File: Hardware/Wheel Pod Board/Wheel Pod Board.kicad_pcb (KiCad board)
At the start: 2 copper layers, 63.5 x 25.5 mm, 30 parts, among them J1 Conn_RJ-45, P1 UIM240XX_Stepper_Conn, P2 RS232, P3 ST_SWD_Connector, P4 SyRen, P5 BATT, U1 STM32F401RCT6, U2 SN75176BDR, U3 ZXCT1107, U4 ZXCT1107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

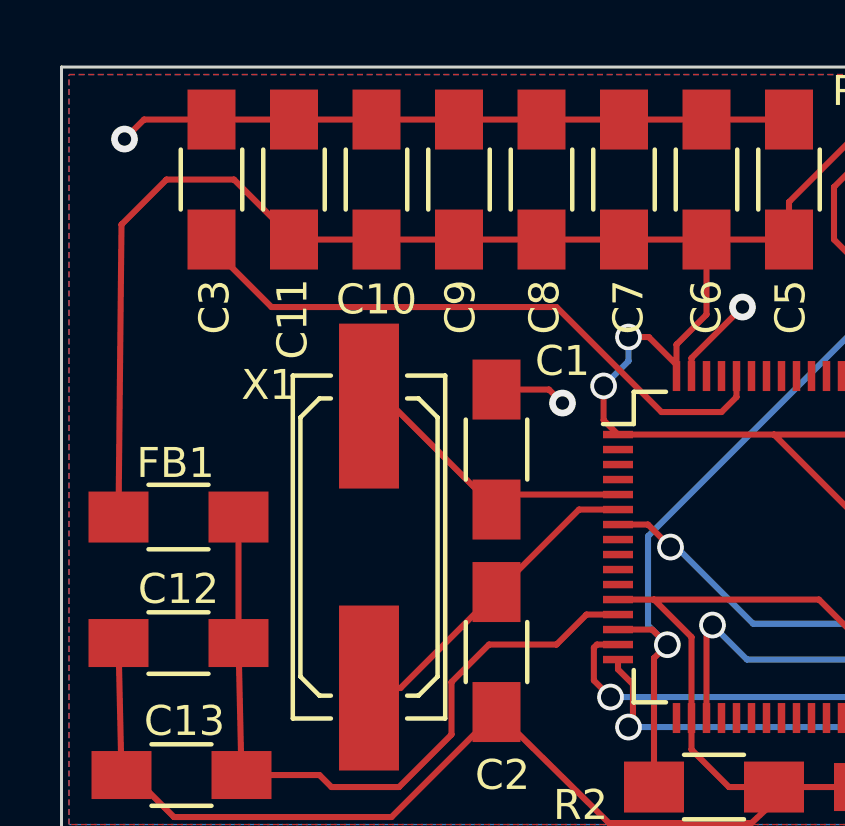
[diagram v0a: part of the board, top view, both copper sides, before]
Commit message: Add red and green LEDs to board
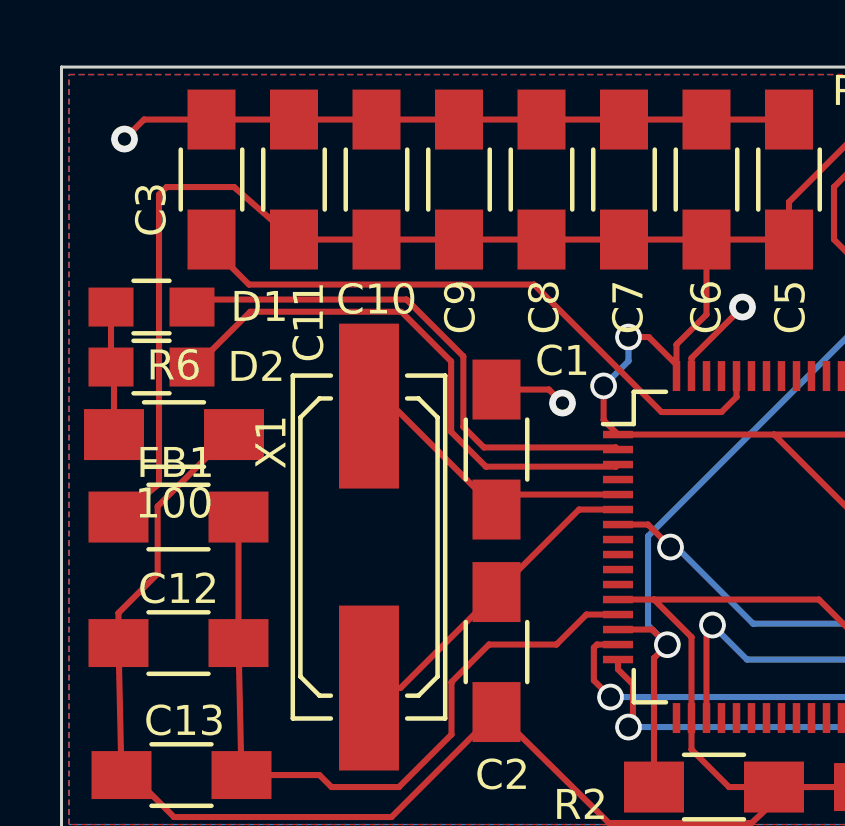
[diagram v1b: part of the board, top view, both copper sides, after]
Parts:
- added D1: LED Red, Resistors_SMD:R_0805_HandSoldering, F.Cu at (222.7, 136.8)
- added D2: LED Green, Resistors_SMD:R_0805_HandSoldering, F.Cu at (222.7, 138.8)
- added R6: 100, Resistors_SMD:R_1206_HandSoldering, F.Cu at (223.4, 141.1)
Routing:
- net Net-(D2-Pad2): track 0.00 -> 18.5 mm
- net Net-(D1-Pad2): track 0.00 -> 17.8 mm
- net GND: track 119.5 -> 128.2 mm
- net Net-(D1-Pad1): track 0.00 -> 4.29 mm

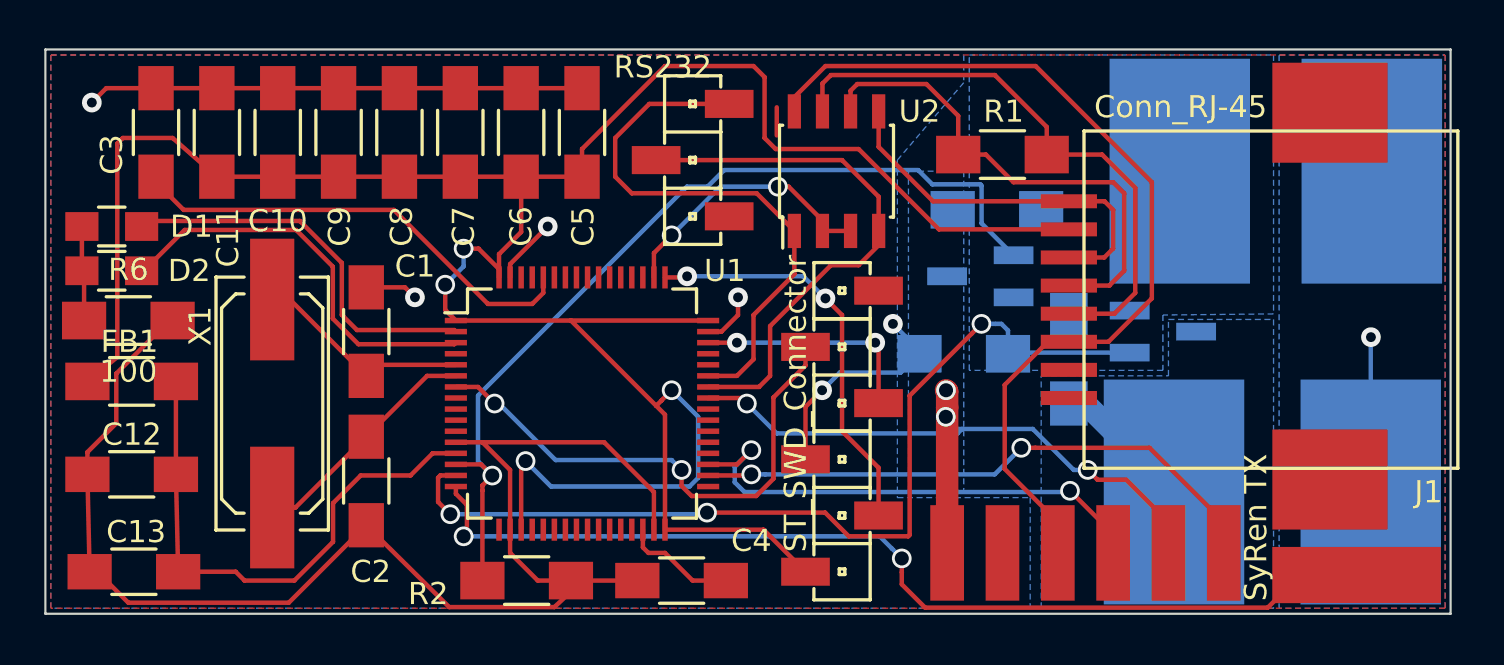
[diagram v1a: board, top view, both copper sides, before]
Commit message: Change out SWD footprint to new breakaway header
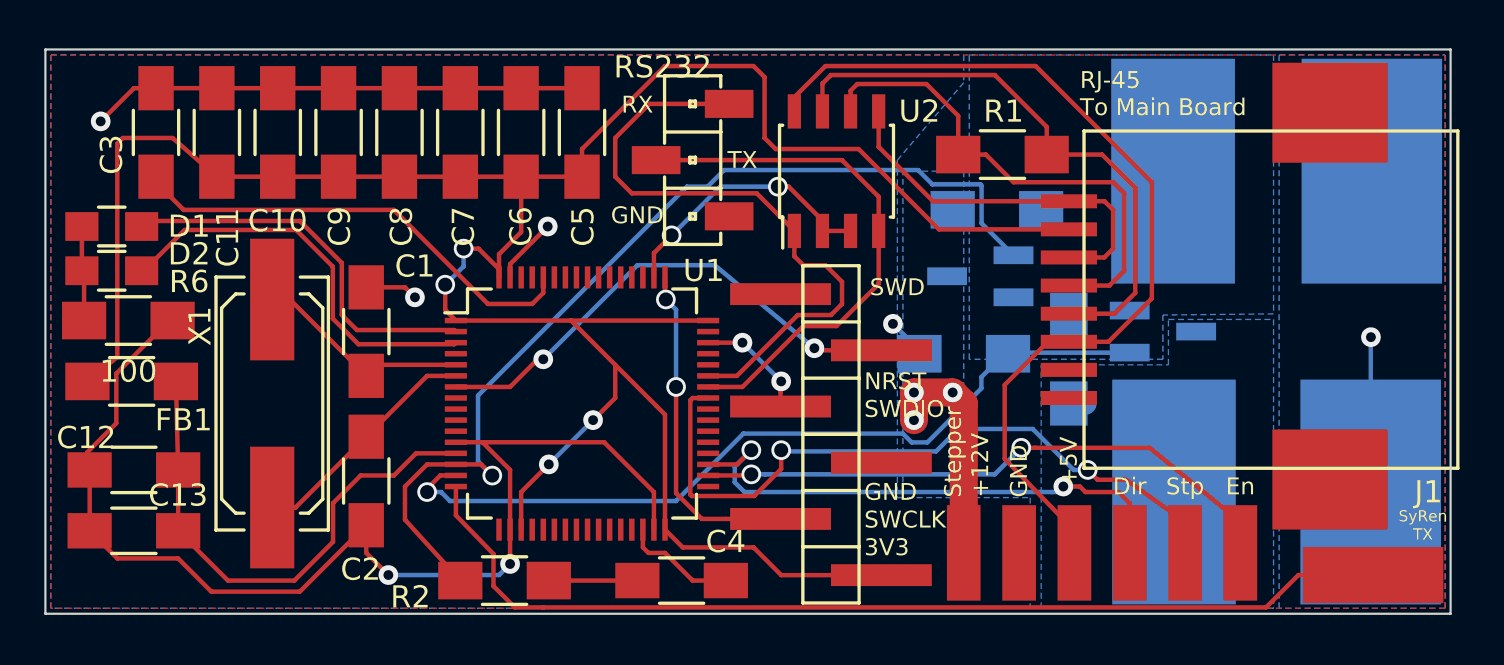
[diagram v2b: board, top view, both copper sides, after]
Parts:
- added ISU MAVRIC: VAL**, MAVRIC_footprints:MAVRIC_LOGO, B.Cu at (229.2, 138.8)
- P3: value ST_SWD_Connector -> SWD; footprint MAVRIC_footprints:1x6_SMD_header -> MAVRIC_footprints:1x6_Breakaway_Header
- moved P3 7.02 mm to (255.2, 153.1)
- moved C13 1.85 mm to (223.7, 150.6)
- moved R2 1.00 mm to (240.4, 152.8)
- moved P1 0.75 mm to (267.2, 151.6)
- moved C12 0.22 mm to (223.7, 147.8)
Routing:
- net GND: track 128.2 -> 112.8 mm
- net /Step_Step: track 25.1 -> 32.3 mm
- net /SyRenCurrent: track 42.8 -> 37.0 mm, vias 3 -> 1
- net Net-(P4-Pad2): track 6.41 -> 0.75 mm
- net /SWDIO: track 10.3 -> 5.51 mm
- net +3V3: track 120.6 -> 116.2 mm
- net /SWCLK: track 18.5 -> 15.2 mm
- net /USART1_RX: track 25.6 -> 28.8 mm
- net /StepperCurrent: track 41.7 -> 44.7 mm
- net /Stp+12V: track 7.82 -> 10.5 mm, vias 2 -> 3
- net /Step_Direction: track 22.9 -> 25.5 mm
- net +5V: track 41.7 -> 43.3 mm
- net (no net): track 1.27 -> 0.00 mm
- net /VDDA: track 24.7 -> 23.6 mm
- net /NRST: track 23.7 -> 22.9 mm
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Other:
- board text added: "+5V"
- board text added: "3V3"
- board text added: "Batt 12V"
- board text added: "Dir"
- board text added: "En"
- board text added: "GND"
- board text added: "MAVRIC Wheel Pod Board V.1 3/7/2015"
- board text added: "NRST"
- board text added: "RJ-45 To Main Board"
- board text added: "RX"
- board text added: "SWCLK"
- board text added: "SWD"
- board text added: "SWDIO"
- board text added: "Stepper +12V"
- board text added: "Stp"
- board text added: "SyRen 12V"
- board text added: "TX"

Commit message: Change 232 header to new breakaway footprint
what a mess
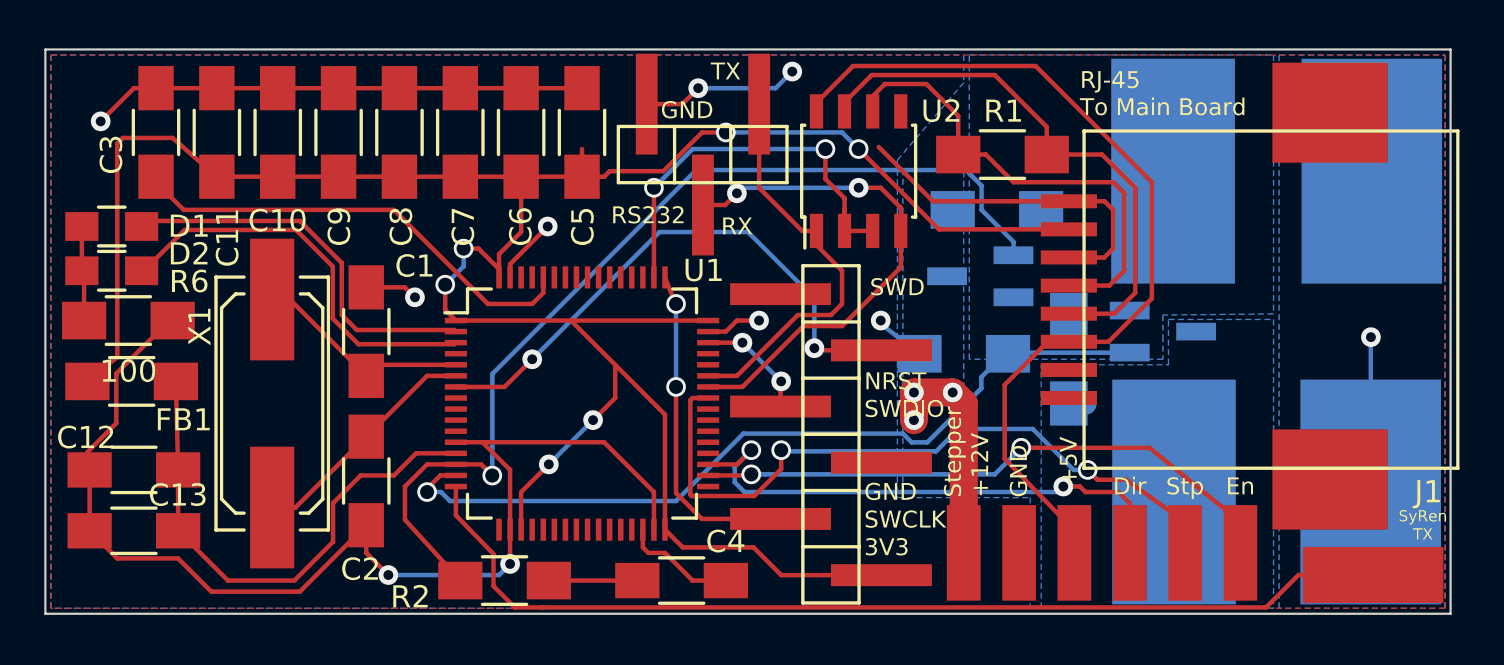
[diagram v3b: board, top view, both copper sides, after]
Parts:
- P2: footprint MAVRIC_footprints:1x3_SMD_header -> MAVRIC_footprints:1x3_Breakaway_Header
- moved P2 3.51 mm to (252.4, 133.6), turned to 180 degrees
- moved U2 1.00 mm to (256.4, 134.3)
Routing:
- net /USART1_RX: track 28.8 -> 18.4 mm
- net /TX_EN: track 12.3 -> 19.2 mm
- net GND: track 112.8 -> 119.4 mm, vias 7 -> 10
- net +3V3: track 116.2 -> 112.6 mm, vias 4 -> 6
- net /NRST: track 22.9 -> 25.7 mm
- net Net-(J1-Pad4): track 27.0 -> 25.5 mm
- net Net-(J1-Pad5): track 24.0 -> 22.8 mm
- net /USART1_TX: track 25.0 -> 23.9 mm, vias 0 -> 2
- net +5V: track 43.3 -> 42.8 mm

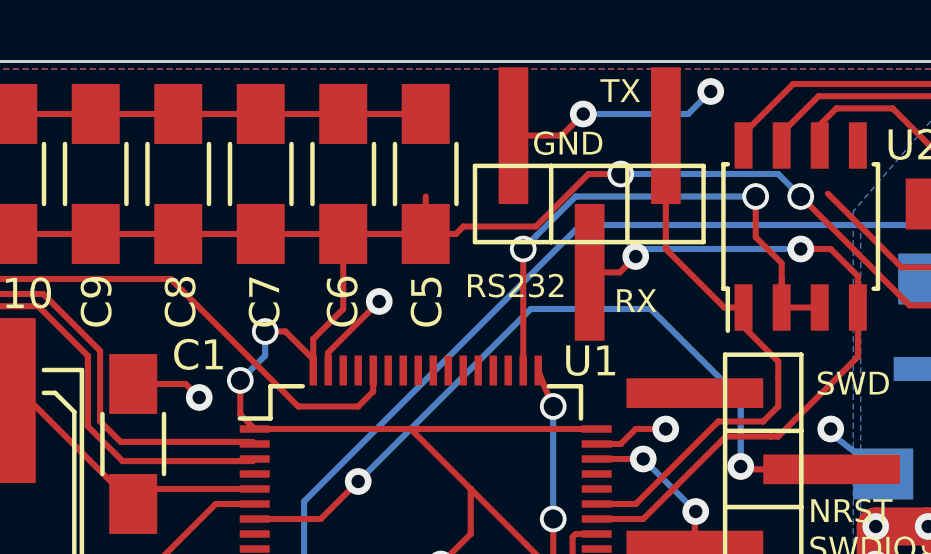
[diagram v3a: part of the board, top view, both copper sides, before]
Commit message: Add pads for connecting encoder
Schematic, PCB, and in cube
Resolves #16
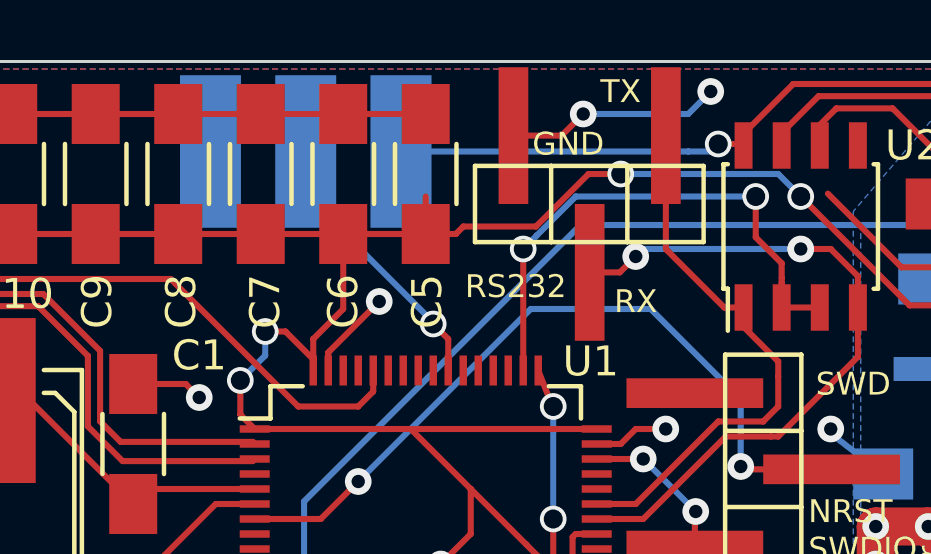
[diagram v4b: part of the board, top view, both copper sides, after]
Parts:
- added J2: M3 Encoder, Wire_Pads:SolderWirePad_3x_0-8mmDrill, B.Cu at (239.9, 131.8)
- P3: value SWD -> ST_SWD_Connector
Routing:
- net +5V: track 42.8 -> 54.6 mm, vias 0 -> 1
- net Net-(J2-Pad2): track 0.00 -> 9.27 mm, vias 0 -> 1
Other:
- board text added: "Encoder"
- board text added: "PWM"

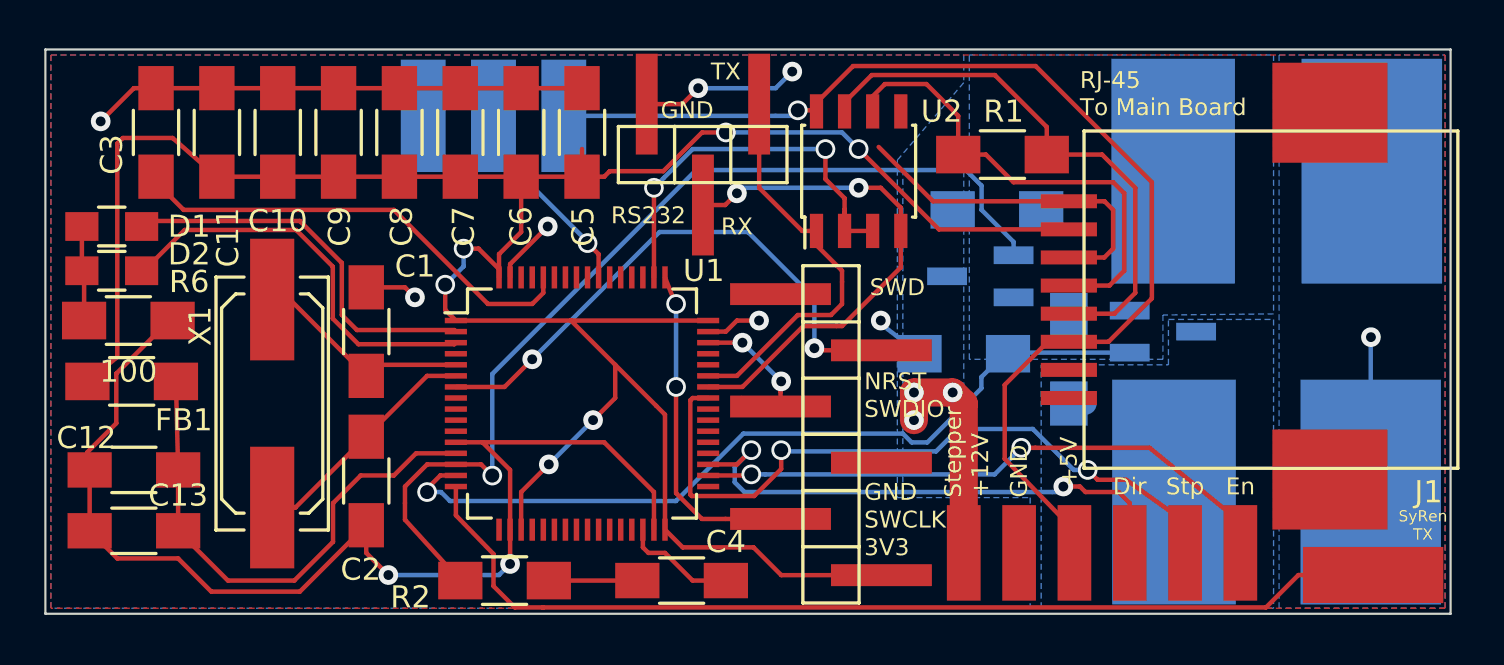
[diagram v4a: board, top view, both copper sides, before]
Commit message: Add resistor for green LED, clean up references
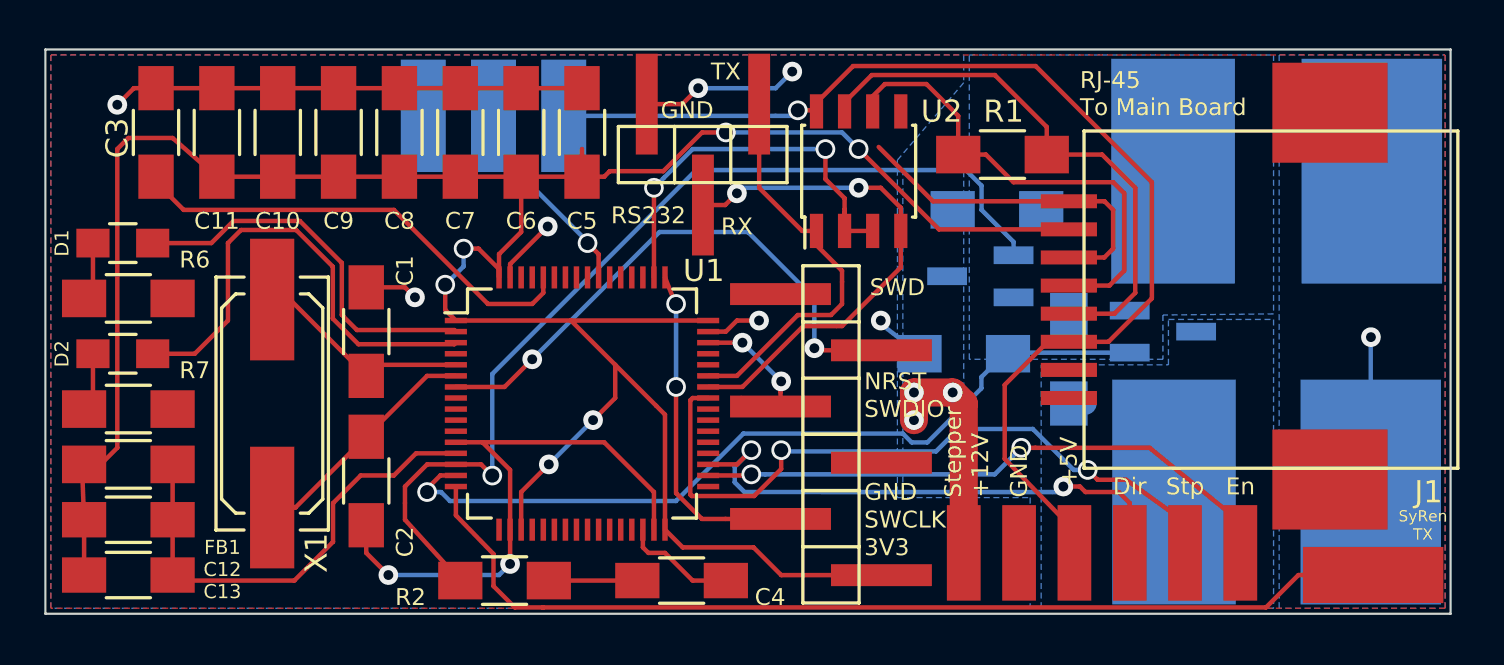
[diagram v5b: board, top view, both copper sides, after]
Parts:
- added R7: 100, Resistors_SMD:R_1206_HandSoldering, F.Cu at (223.4, 145.1)
- moved D2 3.78 mm to (223.2, 142.6)
- moved FB1 3.75 mm to (223.4, 147.6)
- moved C12 2.26 mm to (223.4, 150.1)
- moved C13 2.02 mm to (223.4, 152.6)
- moved R6 1.00 mm to (223.4, 140.1)
- moved D1 0.90 mm to (223.2, 137.6)
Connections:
- D2 pad 1: Net-(D1-Pad1) -> Net-(D2-Pad1)
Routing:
- net GND: track 119.4 -> 94.9 mm
- net +3V3: track 112.6 -> 119.2 mm
- net Net-(D2-Pad2): track 18.5 -> 21.7 mm
- net Net-(D2-Pad1): track 0.00 -> 2.81 mm
- net /VDDA: track 23.6 -> 21.3 mm
- net Net-(D1-Pad1): track 4.29 -> 2.81 mm
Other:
- board text added: "MAVRIC Wheel Pod Board V.1 3/9/2015"
- board text removed: "MAVRIC Wheel Pod Board V.1 3/7/2015"

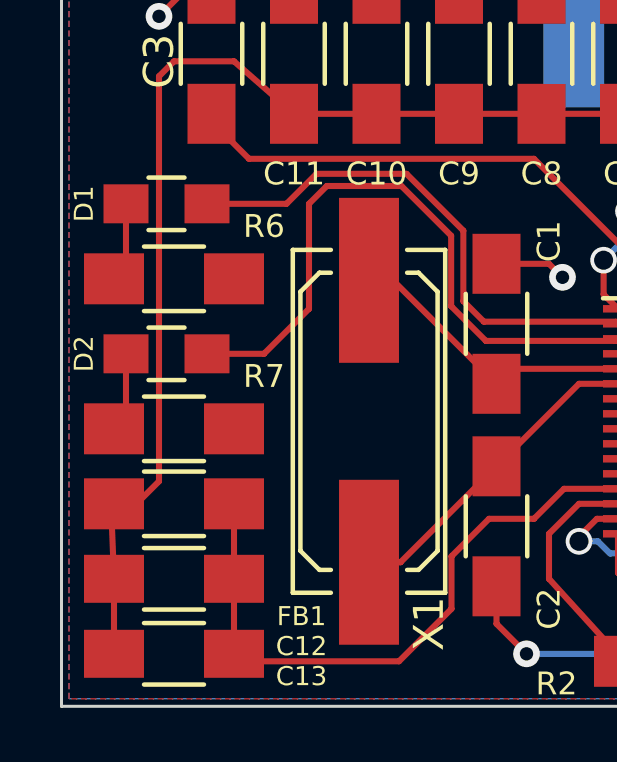
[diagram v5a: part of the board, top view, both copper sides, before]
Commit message: Fix LED polarity
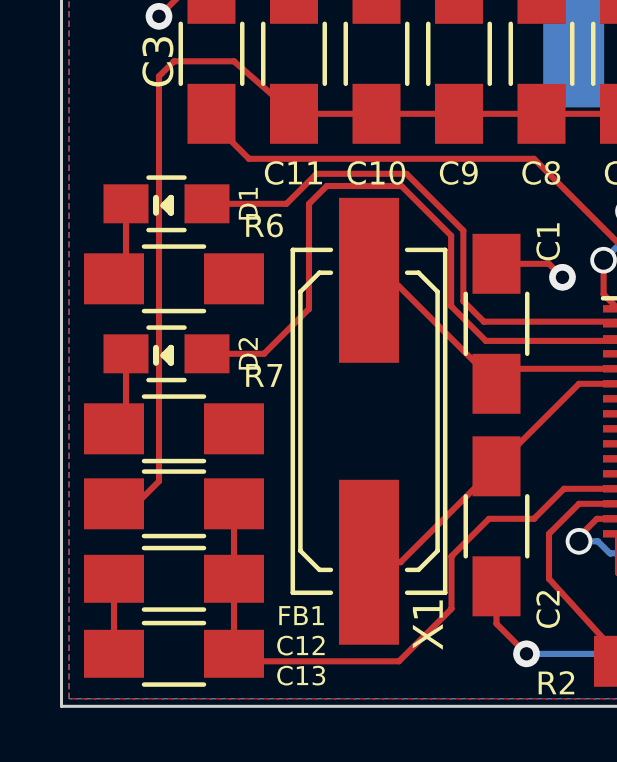
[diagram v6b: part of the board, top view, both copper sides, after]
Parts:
- turned D1 to 180 degrees
- turned D2 to 180 degrees
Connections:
- R6 pad 1: Net-(D1-Pad1) -> Net-(D1-Pad2)
- R7 pad 2: Net-(D2-Pad1) -> Net-(D2-Pad2)
- U1 pad 2: Net-(D1-Pad2) -> Net-(D1-Pad1)
- U1 pad 3: Net-(D2-Pad2) -> Net-(D2-Pad1)
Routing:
- net Net-(D2-Pad2): track 21.7 -> 2.67 mm
- net Net-(D2-Pad1): track 2.81 -> 21.7 mm
- net Net-(D1-Pad2): track 17.9 -> 2.81 mm
- net Net-(D1-Pad1): track 2.81 -> 17.9 mm
- net +3V3: track 119.2 -> 116.6 mm
